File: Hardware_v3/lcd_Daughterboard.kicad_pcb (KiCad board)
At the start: 2 copper layers, 68 x 45 mm, 5 parts, among them J3 Conn_01x03_Pin, J4 Conn_01x03_Pin, J5 Conn_01x02_Pin, J6 Conn_01x02_Pin, U1 ILI9341_SPI_Bare

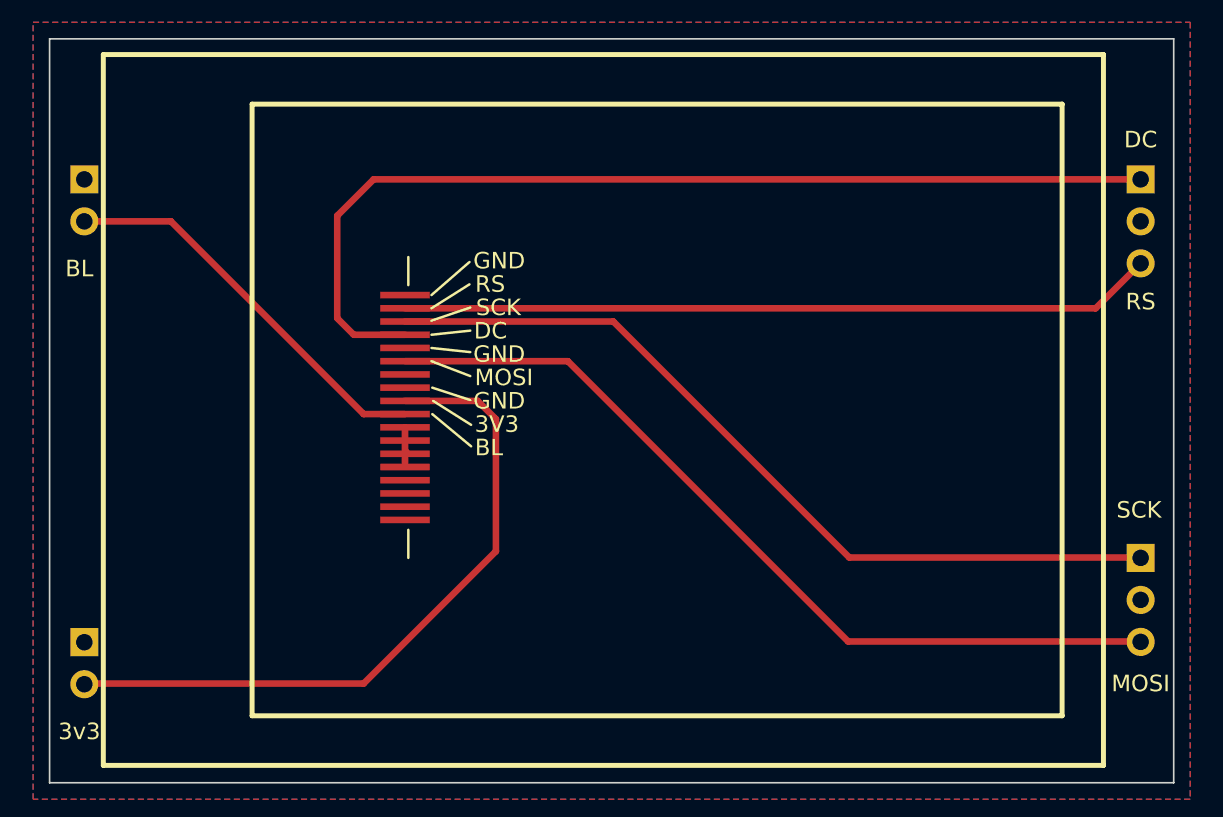
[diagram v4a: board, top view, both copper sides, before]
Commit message: New 3.1 daughterboard layout
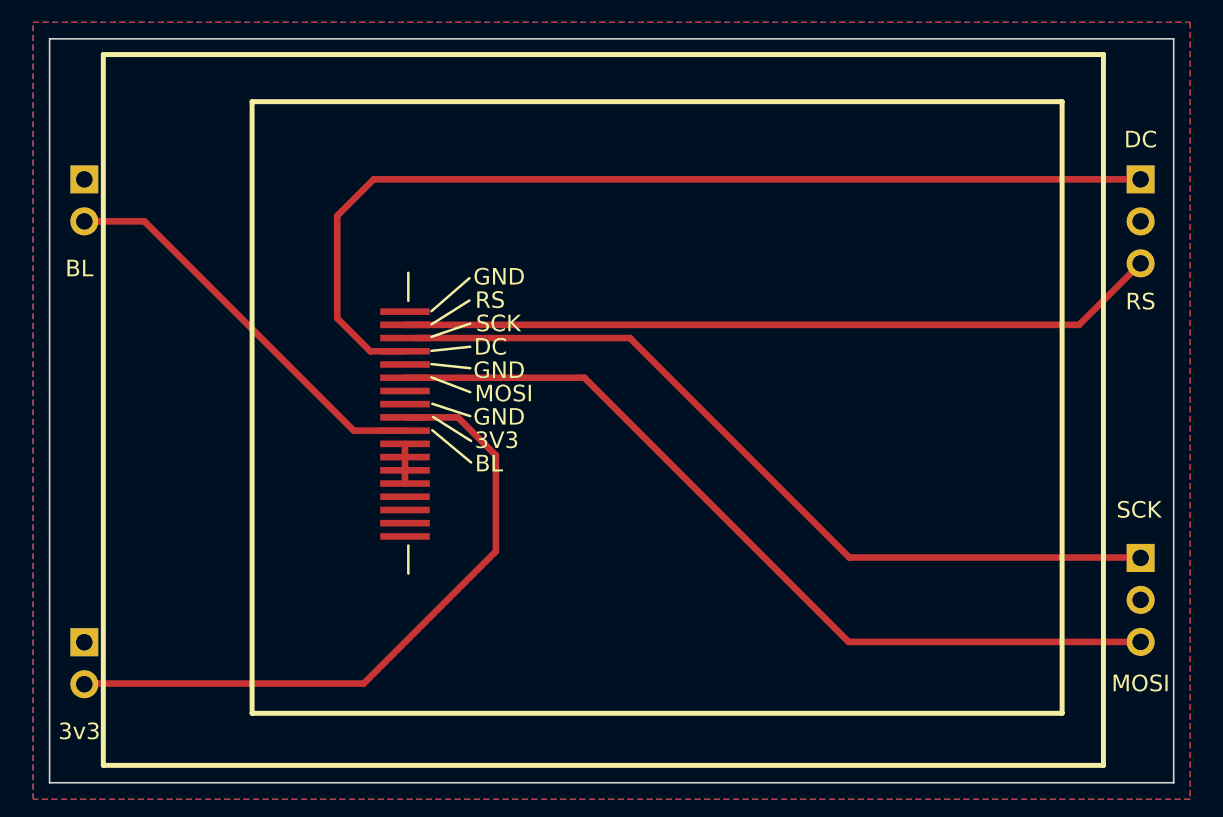
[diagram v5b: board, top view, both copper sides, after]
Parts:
- moved U1 1.00 mm to (121.5, 61.7)
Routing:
- net +3.3V: track 42.2 -> 40.5 mm
- net /LCD_SCK: track 50.4 -> 49.4 mm
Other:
- board text added: "LCD Daughterboard v3.1"
- board text removed: "LCD Daughterboard v3"
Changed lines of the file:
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@@
 	(footprint "Custom_Footprints:18x0.8mmLCDConnector"
 		(layer "F.Cu")
-		(at 121.5 60.7 -90)
+		(at 121.5 61.7 -90)
 		(property "Reference" "U1"
 			(at 15.2 -0.1 0)
@@
 	)
 	(gr_line
-		(start 123.2 67.1)
-		(end 125.5 68.55)
+		(start 123.2 68.075)
+		(end 125.5 69.525)
 		(stroke
 			(width 0.15)
@@
 	)
 	(gr_line
-		(start 123.1 60.7)
-		(end 125.4 58.7)
+		(start 123.1 61.675)
+		(end 125.4 59.675)
 		(stroke
 			(width 0.15)
@@
 	)
 	(gr_line
-		(start 121.7 74.9)
-		(end 121.7 76.6)
+		(start 121.7 75.85)
+		(end 121.7 77.55)
 		(stroke
 			(width 0.15)
@@
 	)
 	(gr_line
-		(start 123.1 63.9)
-		(end 125.45 64.15)
+		(start 123.1 64.875)
+		(end 125.45 65.125)
 		(stroke
 			(width 0.15)
@@
 	)
 	(gr_line
-		(start 123.15 67.9)
-		(end 125.5 69.85)
+		(start 123.15 68.875)
+		(end 125.5 70.825)
 		(stroke
 			(width 0.15)
@@
 	)
 	(gr_line
-		(start 123.15 66.3)
-		(end 125.45 67.05)
+		(start 123.15 67.275)
+		(end 125.45 68.025)
 		(stroke
 			(width 0.15)
@@
 	)
 	(gr_line
-		(start 121.7 58.4)
-		(end 121.7 60.1)
+		(start 121.7 59.35)
+		(end 121.7 61.05)
 		(stroke
 			(width 0.15)
@@
 	)
 	(gr_line
-		(start 123.1 64.7)
-		(end 125.45 65.6)
+		(start 123.1 65.675)
+		(end 125.45 66.575)
 		(stroke
 			(width 0.15)
@@
 	)
 	(gr_rect
-		(start 112.25 49.15)
-		(end 161.25 86.15)
+		(start 112.25 49)
+		(end 161.25 86)
 		(stroke
 			(width 0.3)
@@
 	)
 	(gr_line
-		(start 123.1 61.5)
-		(end 125.4 60.05)
+		(start 123.1 62.475)
+		(end 125.4 61.025)
 		(stroke
 			(width 0.15)
@@
 	)
 	(gr_line
-		(start 123.1 63.1)
-		(end 125.45 62.85)
+		(start 123.1 64.075)
+		(end 125.45 63.825)
 		(stroke
 			(width 0.15)
@@
 	)
 	(gr_line
-		(start 123.1 62.25)
-		(end 125.45 61.45)
+		(start 123.1 63.225)
+		(end 125.45 62.425)
 		(stroke
 			(width 0.15)
@@
 	)
 	(gr_rect
-		(start 112.25 49.15)
-		(end 161.25 86.15)
+		(start 112.25 49)
+		(end 161.25 86)
 		(stroke
 			(width 0.2)
@@
 		(layer "Edge.Cuts")
 	)
-	(gr_text "LCD Daughterboard v3"
+	(gr_text "LCD Daughterboard v3.1"
 		(at 135.4 47.3 0)
 		(layer "B.SilkS")
@@
 	)
 	(gr_text "3V3"
-		(at 127.054762 68.5125 0)
+		(at 127.054762 69.4875 0)
 		(layer "F.SilkS")
 		(effects
@@
 	)
 	(gr_text "DC"
-		(at 126.67381 62.8625 0)
+		(at 126.67381 63.8375 0)
 		(layer "F.SilkS")
 		(effects
@@
 	)
 	(gr_text "GND"
-		(at 127.197619 64.275 0)
+		(at 127.197619 65.25 0)
 		(layer "F.SilkS")
 		(effects
@@
 	)
 	(gr_text "GND"
-		(at 127.197619 67.1 0)
+		(at 127.197619 68.075 0)
 		(layer "F.SilkS")
 		(effects
@@
 	)
 	(gr_text "MOSI"
-		(at 127.483333 65.6875 0)
+		(at 127.483333 66.6625 0)
 		(layer "F.SilkS")
 		(effects
@@
 	)
 	(gr_text "BL"
-		(at 126.578572 69.925 0)
+		(at 126.578572 70.9 0)
 		(layer "F.SilkS")
 		(effects
@@
 	)
 	(gr_text "GND"
-		(at 127.197619 58.625 0)
+		(at 127.197619 59.6 0)
 		(layer "F.SilkS")
 		(effects
@@
 	)
 	(gr_text "RS"
-		(at 126.65 60.0375 0)
+		(at 126.65 61.0125 0)
 		(layer "F.SilkS")
 		(effects
@@
 	)
 	(gr_text "SCK"
-		(at 127.15 61.45 0)
+		(at 127.15 62.425 0)
 		(layer "F.SilkS")
 		(effects
@@
 	)
 	(segment
-		(start 121.6 70.2)
-		(end 121.5 70.3)
+		(start 121.5 72.1)
+		(end 121.5 69.7)
 		(width 0.4)
 		(layer "F.Cu")
@@
 	)
 	(segment
-		(start 121.5 71.1)
-		(end 121.5 68.7)
-		(width 0.4)
-		(layer "F.Cu")
-		(net 1)
-	)
-	(segment
-		(start 125.9 67.1)
-		(end 127 68.2)
+		(start 127 70.4)
+		(end 127 76.2)
+		(width 0.4)
+		(layer "F.Cu")
+		(net 3)
+	)
+	(segment
+		(start 121.5 68.1)
+		(end 124.7 68.1)
+		(width 0.4)
+		(layer "F.Cu")
+		(net 3)
+	)
+	(segment
+		(start 119 84.2)
+		(end 102.1 84.2)
 		(width 0.4)
 		(layer "F.Cu")
@@
 	)
 	(segment
-		(start 127 68.2)
-		(end 127 76.2)
+		(start 124.7 68.1)
+		(end 127 70.4)
 		(width 0.4)
 		(layer "F.Cu")
@@
 	)
 	(segment
-		(start 121.5 67.1)
-		(end 125.9 67.1)
-		(width 0.4)
-		(layer "F.Cu")
-		(net 3)
-	)
-	(segment
-		(start 119 84.2)
-		(end 102.1 84.2)
-		(width 0.4)
-		(layer "F.Cu")
-		(net 3)
-	)
-	(segment
-		(start 118.4 63.1)
+		(start 117.4 55.9)
+		(end 119.6 53.7)
+		(width 0.4)
+		(layer "F.Cu")
+		(net 5)
+	)
+	(segment
+		(start 119.6 53.7)
+		(end 166 53.7)
+		(width 0.4)
+		(layer "F.Cu")
+		(net 5)
+	)
+	(segment
+		(start 119.4 64.1)
 		(end 117.4 62.1)
 		(width 0.4)
@@
 	)
 	(segment
-		(start 119.6 53.7)
-		(end 166 53.7)
+		(start 121.5 64.1)
+		(end 119.4 64.1)
 		(width 0.4)
 		(layer "F.Cu")
@@
 	)
 	(segment
-		(start 117.4 55.9)
-		(end 119.6 53.7)
-		(width 0.4)
-		(layer "F.Cu")
-		(net 5)
-	)
-	(segment
-		(start 121.5 63.1)
-		(end 118.4 63.1)
-		(width 0.4)
-		(layer "F.Cu")
-		(net 5)
-	)
-	(segment
-		(start 121.5 61.5)
-		(end 163.28 61.5)
+		(start 162.28 62.5)
+		(end 166 58.78)
 		(width 0.4)
 		(layer "F.Cu")
@@
 	)
 	(segment
-		(start 163.28 61.5)
-		(end 166 58.78)
+		(start 121.5 62.5)
+		(end 162.28 62.5)
 		(width 0.4)
 		(layer "F.Cu")
@@
 	)
 	(segment
-		(start 121.5 64.7)
-		(end 131.351472 64.7)
+		(start 132.351472 65.7)
+		(end 148.331472 81.68)
 		(width 0.4)
 		(layer "F.Cu")
@@
 	)
 	(segment
-		(start 148.306472 81.655)
-		(end 165.975 81.655)
+		(start 121.5 65.7)
+		(end 132.351472 65.7)
 		(width 0.4)
 		(layer "F.Cu")
@@
 	)
 	(segment
-		(start 131.351472 64.7)
-		(end 148.306472 81.655)
+		(start 148.331472 81.68)
+		(end 166 81.68)
 		(width 0.4)
 		(layer "F.Cu")
@@
 	)
 	(segment
-		(start 165.975 81.655)
-		(end 166 81.68)
-		(width 0.4)
-		(layer "F.Cu")
-		(net 8)
-	)
-	(segment
-		(start 121.5 67.9)
-		(end 119 67.9)
+		(start 105.74 56.24)
+		(end 118.4 68.9)
 		(width 0.4)
 		(layer "F.Cu")
@@
 	)
 	(segment
-		(start 119 67.9)
-		(end 107.34 56.24)
+		(start 102.1 56.24)
+		(end 105.74 56.24)
 		(width 0.4)
 		(layer "F.Cu")
@@
 	)
 	(segment
-		(start 107.34 56.24)
-		(end 102.1 56.24)
+		(start 118.4 68.9)
+		(end 121.5 68.9)
 		(width 0.4)
 		(layer "F.Cu")
@@
 	)
 	(segment
-		(start 134.1 62.3)
-		(end 148.375 76.575)
+		(start 122.1 63.3)
+		(end 135.1 63.3)
 		(width 0.4)
 		(layer "F.Cu")
@@
 	)
 	(segment
-		(start 121.5 62.3)
-		(end 134.1 62.3)
+		(start 148.375 76.575)
+		(end 165.975 76.575)
 		(width 0.4)
 		(layer "F.Cu")
@@
 	)
 	(segment
-		(start 148.375 76.575)
-		(end 165.975 76.575)
-		(width 0.4)
-		(layer "F.Cu")
+		(start 135.1 63.3)
+		(end 148.375 76.575)
+		(width 0.4)
+		(layer "F.Cu")

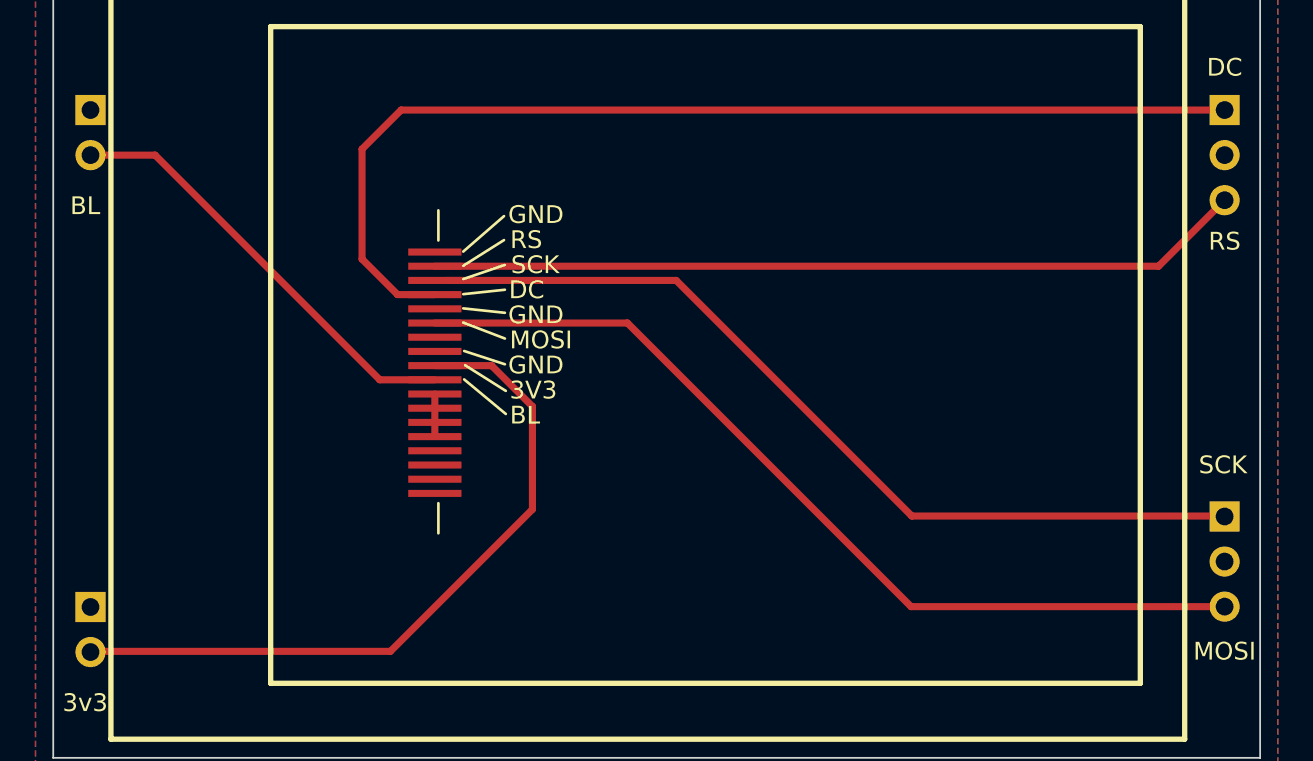
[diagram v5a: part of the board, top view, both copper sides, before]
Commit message: UI fixes; minor tweaks to v3.2 LCD daughterboard
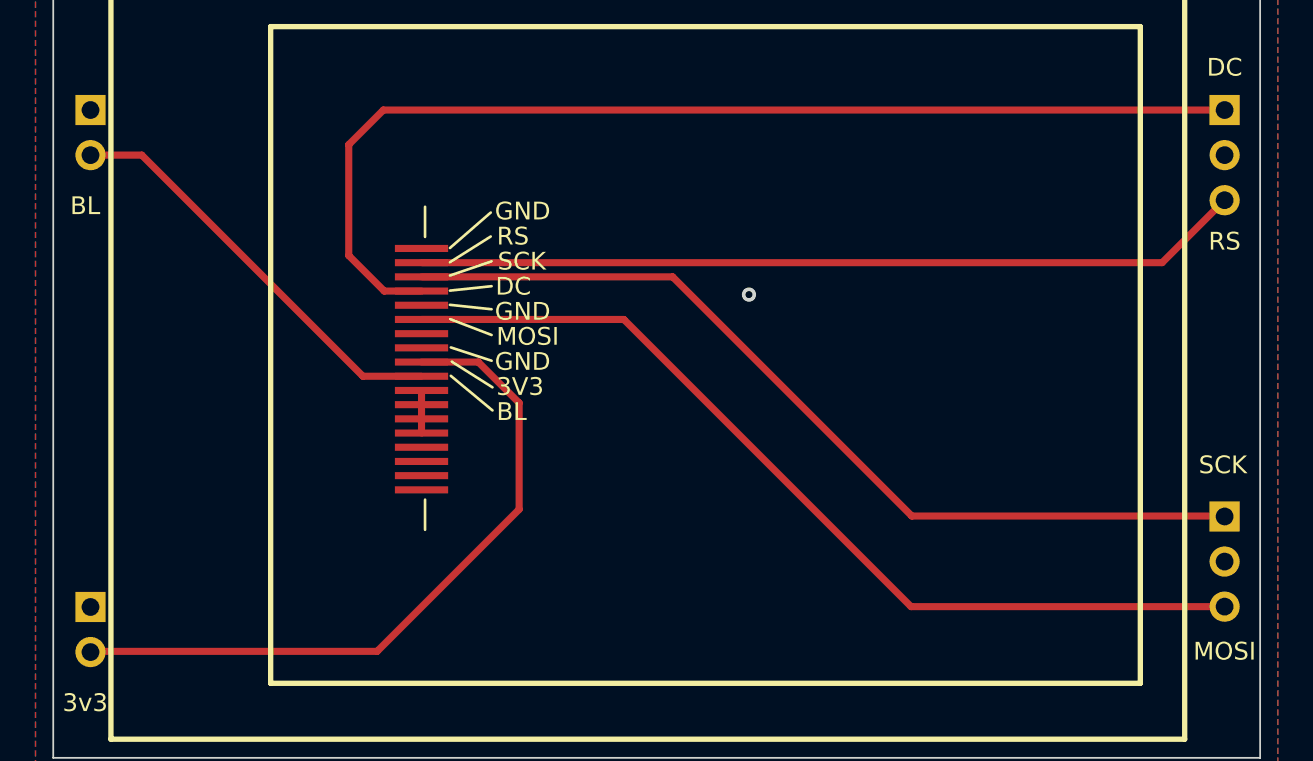
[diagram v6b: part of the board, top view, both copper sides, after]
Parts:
- moved U1 0.78 mm to (120.8, 61.5)
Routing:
- net /LCD_SCK: track 49.4 -> 50.8 mm
- net /LCD_MOSI: track 51.1 -> 52.0 mm
- net /BackLight: track 24.6 -> 23.8 mm
- net /LCD_DC: track 60.6 -> 61.3 mm
- net /LCD_RESET: track 46.0 -> 46.7 mm
- net +3.3V: track 40.5 -> 39.9 mm
- net GND: vias 0 -> 1
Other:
- board text added: "LCD Daughterboard v3.2 Mountjoy Modular"
- board text removed: "LCD Daughterboard v3.1"
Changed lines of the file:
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@@
 	(footprint "Custom_Footprints:18x0.8mmLCDConnector"
 		(layer "F.Cu")
-		(at 121.5 61.7 -90)
+		(at 120.75 61.5 -90)
 		(property "Reference" "U1"
 			(at 15.2 -0.1 0)
@@
 	)
 	(gr_line
-		(start 123.2 68.075)
-		(end 125.5 69.525)
+		(start 122.45 67.875)
+		(end 124.75 69.325)
 		(stroke
 			(width 0.15)
@@
 	)
 	(gr_line
-		(start 123.1 61.675)
-		(end 125.4 59.675)
+		(start 122.35 61.475)
+		(end 124.65 59.475)
 		(stroke
 			(width 0.15)
@@
 	)
 	(gr_line
-		(start 121.7 75.85)
-		(end 121.7 77.55)
+		(start 120.95 75.65)
+		(end 120.95 77.35)
 		(stroke
 			(width 0.15)
@@
 	)
 	(gr_line
-		(start 123.1 64.875)
-		(end 125.45 65.125)
+		(start 122.35 64.675)
+		(end 124.7 64.925)
 		(stroke
 			(width 0.15)
@@
 	)
 	(gr_line
-		(start 123.15 68.875)
-		(end 125.5 70.825)
+		(start 122.4 68.675)
+		(end 124.75 70.625)
 		(stroke
 			(width 0.15)
@@
 	)
 	(gr_line
-		(start 123.15 67.275)
-		(end 125.45 68.025)
+		(start 122.4 67.075)
+		(end 124.7 67.825)
 		(stroke
 			(width 0.15)
@@
 	)
 	(gr_line
-		(start 121.7 59.35)
-		(end 121.7 61.05)
+		(start 120.95 59.15)
+		(end 120.95 60.85)
 		(stroke
 			(width 0.15)
@@
 	)
 	(gr_line
-		(start 123.1 65.675)
-		(end 125.45 66.575)
+		(start 122.35 65.475)
+		(end 124.7 66.375)
 		(stroke
 			(width 0.15)
@@
 	)
 	(gr_line
-		(start 123.1 62.475)
-		(end 125.4 61.025)
+		(start 122.35 62.275)
+		(end 124.65 60.825)
 		(stroke
 			(width 0.15)
@@
 	)
 	(gr_line
-		(start 123.1 64.075)
-		(end 125.45 63.825)
+		(start 122.35 63.875)
+		(end 124.7 63.625)
 		(stroke
 			(width 0.15)
@@
 	)
 	(gr_line
-		(start 123.1 63.225)
-		(end 125.45 62.425)
+		(start 122.35 63.025)
+		(end 124.7 62.225)
 		(stroke
 			(width 0.15)
@@
 		(layer "Edge.Cuts")
 	)
-	(gr_text "LCD Daughterboard v3.1"
+	(gr_text "LCD Daughterboard v3.2\nMountjoy Modular"
 		(at 135.4 47.3 0)
 		(layer "B.SilkS")
@@
 	)
 	(gr_text "3V3"
-		(at 127.054762 69.4875 0)
+		(at 126.304762 69.2875 0)
 		(layer "F.SilkS")
 		(effects
@@
 	)
 	(gr_text "DC"
-		(at 126.67381 63.8375 0)
+		(at 125.92381 63.6375 0)
 		(layer "F.SilkS")
 		(effects
@@
 	)
 	(gr_text "GND"
-		(at 127.197619 65.25 0)
+		(at 126.447619 65.05 0)
 		(layer "F.SilkS")
 		(effects
@@
 	)
 	(gr_text "GND"
-		(at 127.197619 68.075 0)
+		(at 126.447619 67.875 0)
 		(layer "F.SilkS")
 		(effects
@@
 	)
 	(gr_text "MOSI"
-		(at 127.483333 66.6625 0)
+		(at 126.733333 66.4625 0)
 		(layer "F.SilkS")
 		(effects
@@
 	)
 	(gr_text "BL"
-		(at 126.578572 70.9 0)
+		(at 125.828572 70.7 0)
 		(layer "F.SilkS")
 		(effects
@@
 	)
 	(gr_text "GND"
-		(at 127.197619 59.6 0)
+		(at 126.447619 59.4 0)
 		(layer "F.SilkS")
 		(effects
@@
 	)
 	(gr_text "RS"
-		(at 126.65 61.0125 0)
+		(at 125.9 60.8125 0)
 		(layer "F.SilkS")
 		(effects
@@
 	)
 	(gr_text "SCK"
-		(at 127.15 62.425 0)
+		(at 126.4 62.225 0)
 		(layer "F.SilkS")
 		(effects
@@
 	)
 	(segment
-		(start 121.5 72.1)
-		(end 121.5 69.7)
+		(start 120.75 71.9)
+		(end 120.75 69.5)
 		(width 0.4)
 		(layer "F.Cu")
 		(net 1)
 	)
-	(segment
-		(start 127 70.4)
-		(end 127 76.2)
+	(via
+		(at 139.2 64.1)
+		(size 0.8)
+		(drill 0.4)
+		(layers "F.Cu" "B.Cu")
+		(free yes)
+		(net 1)
+	)
+	(segment
+		(start 120.75 67.9)
+		(end 123.95 67.9)
 		(width 0.4)
 		(layer "F.Cu")
@@
 	)
 	(segment
-		(start 121.5 68.1)
-		(end 124.7 68.1)
+		(start 118.25 84.2)
+		(end 102.1 84.2)
 		(width 0.4)
 		(layer "F.Cu")
@@
 	)
 	(segment
-		(start 119 84.2)
-		(end 102.1 84.2)
+		(start 123.95 67.9)
+		(end 126.25 70.2)
 		(width 0.4)
 		(layer "F.Cu")
@@
 	)
 	(segment
-		(start 127 76.2)
-		(end 119 84.2)
+		(start 126.25 70.2)
+		(end 126.25 76.2)
 		(width 0.4)
 		(layer "F.Cu")
@@
 	)
 	(segment
-		(start 124.7 68.1)
-		(end 127 70.4)
+		(start 126.25 76.2)
+		(end 118.25 84.2)
 		(width 0.4)
 		(layer "F.Cu")
@@
 	)
 	(segment
-		(start 117.4 55.9)
-		(end 119.6 53.7)
+		(start 118.65 63.9)
+		(end 116.65 61.9)
 		(width 0.4)
 		(layer "F.Cu")
@@
 	)
 	(segment
-		(start 119.6 53.7)
+		(start 116.65 61.9)
+		(end 116.65 55.65)
+		(width 0.4)
+		(layer "F.Cu")
+		(net 5)
+	)
+	(segment
+		(start 120.75 63.9)
+		(end 118.65 63.9)
+		(width 0.4)
+		(layer "F.Cu")
+		(net 5)
+	)
+	(segment
+		(start 116.65 55.65)
+		(end 118.6 53.7)
+		(width 0.4)
+		(layer "F.Cu")
+		(net 5)
+	)
+	(segment
+		(start 118.6 53.7)
 		(end 166 53.7)
 		(width 0.4)
@@
 	)
 	(segment
-		(start 119.4 64.1)
-		(end 117.4 62.1)
-		(width 0.4)
-		(layer "F.Cu")
-		(net 5)
-	)
-	(segment
-		(start 117.4 62.1)
-		(end 117.4 55.9)
-		(width 0.4)
-		(layer "F.Cu")
-		(net 5)
-	)
-	(segment
-		(start 121.5 64.1)
-		(end 119.4 64.1)
-		(width 0.4)
-		(layer "F.Cu")
-		(net 5)
-	)
-	(segment
-		(start 162.28 62.5)
+		(start 162.48 62.3)
 		(end 166 58.78)
 		(width 0.4)
@@
 	)
 	(segment
-		(start 121.5 62.5)
-		(end 162.28 62.5)
+		(start 120.75 62.3)
+		(end 162.48 62.3)
 		(width 0.4)
 		(layer "F.Cu")
@@
 	)
 	(segment
-		(start 132.351472 65.7)
+		(start 120.75 65.5)
+		(end 132.151472 65.5)
+		(width 0.4)
+		(layer "F.Cu")
+		(net 8)
+	)
+	(segment
+		(start 132.151472 65.5)
 		(end 148.331472 81.68)
-		(width 0.4)
-		(layer "F.Cu")
-		(net 8)
-	)
-	(segment
-		(start 121.5 65.7)
-		(end 132.351472 65.7)
 		(width 0.4)
 		(layer "F.Cu")
@@
 	)
 	(segment
-		(start 105.74 56.24)
-		(end 118.4 68.9)
+		(start 102.1 56.24)
+		(end 104.99 56.24)
 		(width 0.4)
 		(layer "F.Cu")
@@
 	)
 	(segment
-		(start 102.1 56.24)
-		(end 105.74 56.24)
+		(start 117.45 68.7)
+		(end 120.75 68.7)
 		(width 0.4)
 		(layer "F.Cu")
@@
 	)
 	(segment
-		(start 118.4 68.9)
-		(end 121.5 68.9)
+		(start 104.99 56.24)
+		(end 117.45 68.7)
 		(width 0.4)
 		(layer "F.Cu")
@@
 	)
 	(segment
-		(start 122.1 63.3)
-		(end 135.1 63.3)
+		(start 134.9 63.1)
+		(end 148.375 76.575)
+		(width 0.4)
+		(layer "F.Cu")
+		(net 12)
+	)
+	(segment
+		(start 120.75 63.1)
+		(end 134.9 63.1)
+		(width 0.4)
+		(layer "F.Cu")
+		(net 12)
+	)
+	(segment
+		(start 165.975 76.575)
+		(end 166 76.6)
 		(width 0.4)
 		(layer "F.Cu")
@@
 		(width 0.4)
 		(layer "F.Cu")
-		(net 12)
-	)
-	(segment
-		(start 165.975 76.575)
-		(end 166 76.6)
-		(width 0.4)
-		(layer "F.Cu")
-		(net 12)
-	)
-	(segment
-		(start 135.1 63.3)
-		(end 148.375 76.575)
-		(width 0.4)
-		(layer "F.Cu")
